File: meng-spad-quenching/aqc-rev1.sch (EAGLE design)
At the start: 135 parts, among them IC1 ADCMP582, IC2 NC7SV74K8X, IC3 LT3032-5, IC4 OPA342, IC5 OPA342, IC6 LTC1711, IC7 DS1100LU-20+, IC8 LT3032-15, IC9 NC7WZ16P6X, J1 VIN_LOGIC, M1 BSS806N, Q1 MMBTH81, Q2 MMBTH81, Q3 MMBTH81, Q4 MMBTH81, Q5 MMBTH81, Q6 MMBTH81, T1 MMBTH10, T2 MMBTH10, T3 MMBTH10, T4 MMBTH10, T5 MMBTH10, T6 MMBTH10, T7 MMBTH10, U1 SN65EPT21DGK, U2 TPS78233DDCT, U3 SN65EPT22DGK, X1 CONN_SPAD, X2 CONN_PHOTON_COUNTER, X4 CONN_VREF_ONE_SHOT_EXT, X5 CONN_VREF_DIAMOND_IBIAS_EXT, X6 CONN_VREF_CASCODE_IBIAS_EXT

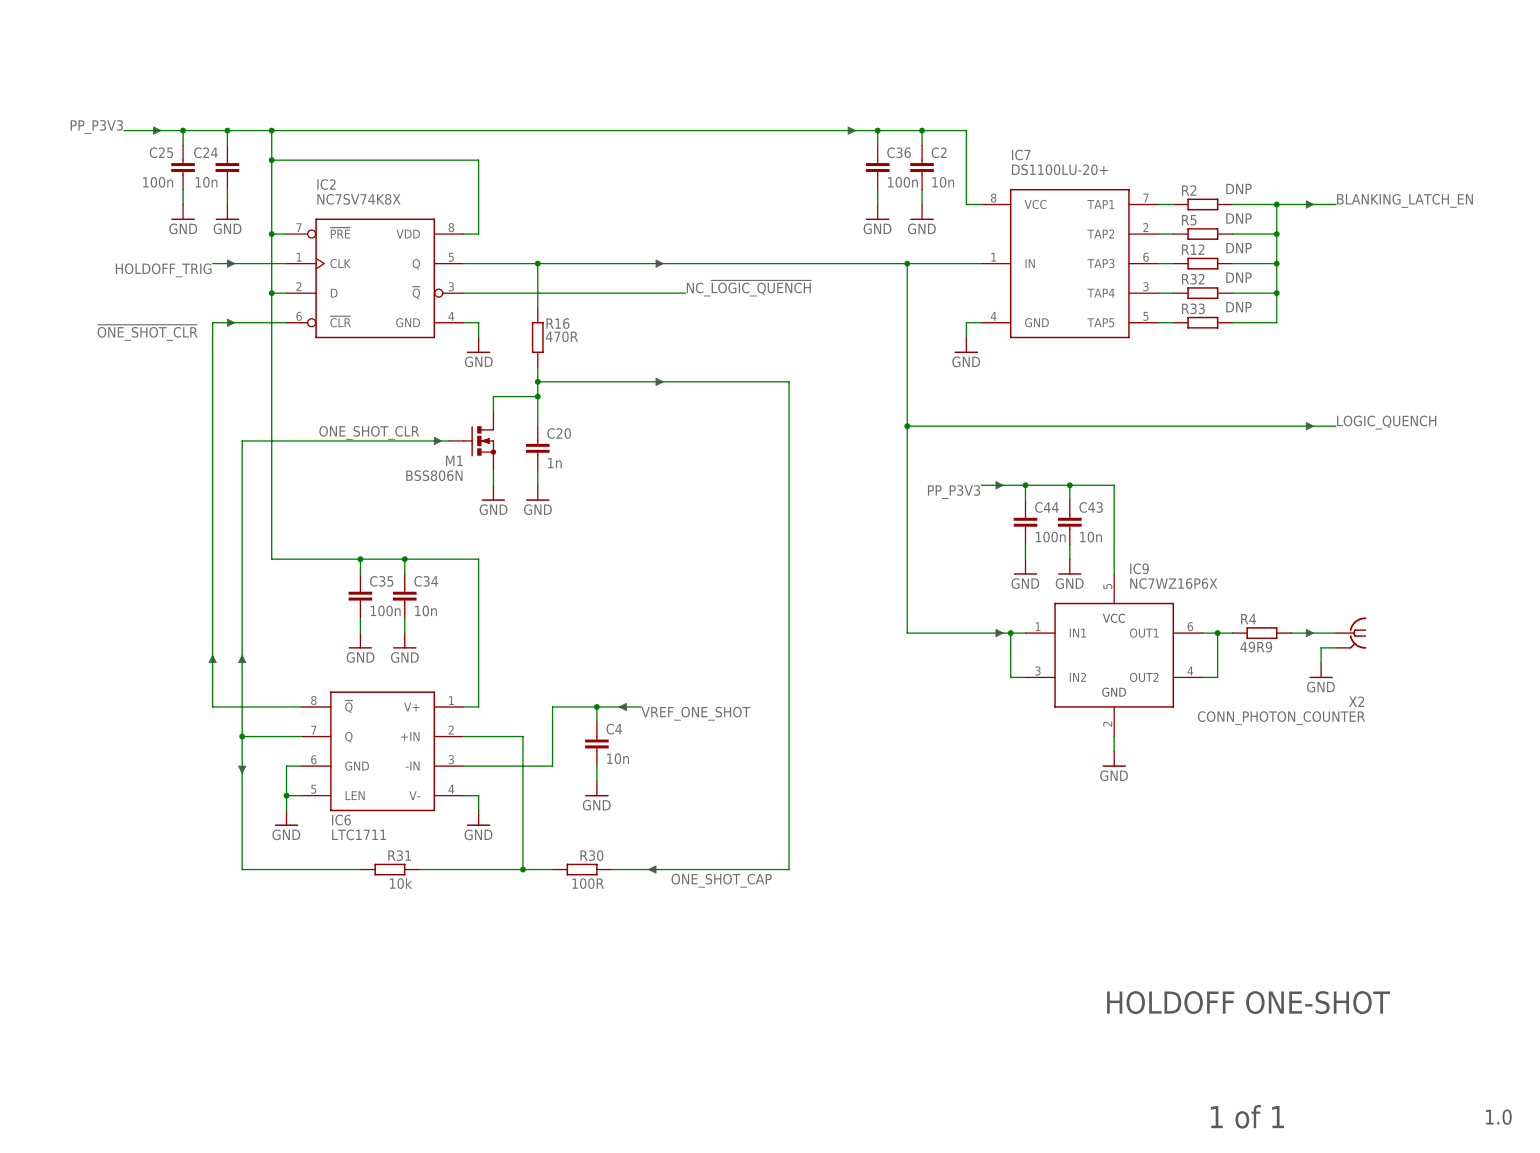
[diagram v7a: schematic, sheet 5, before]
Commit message: Added forced quenching input, finalized connector placement in layout
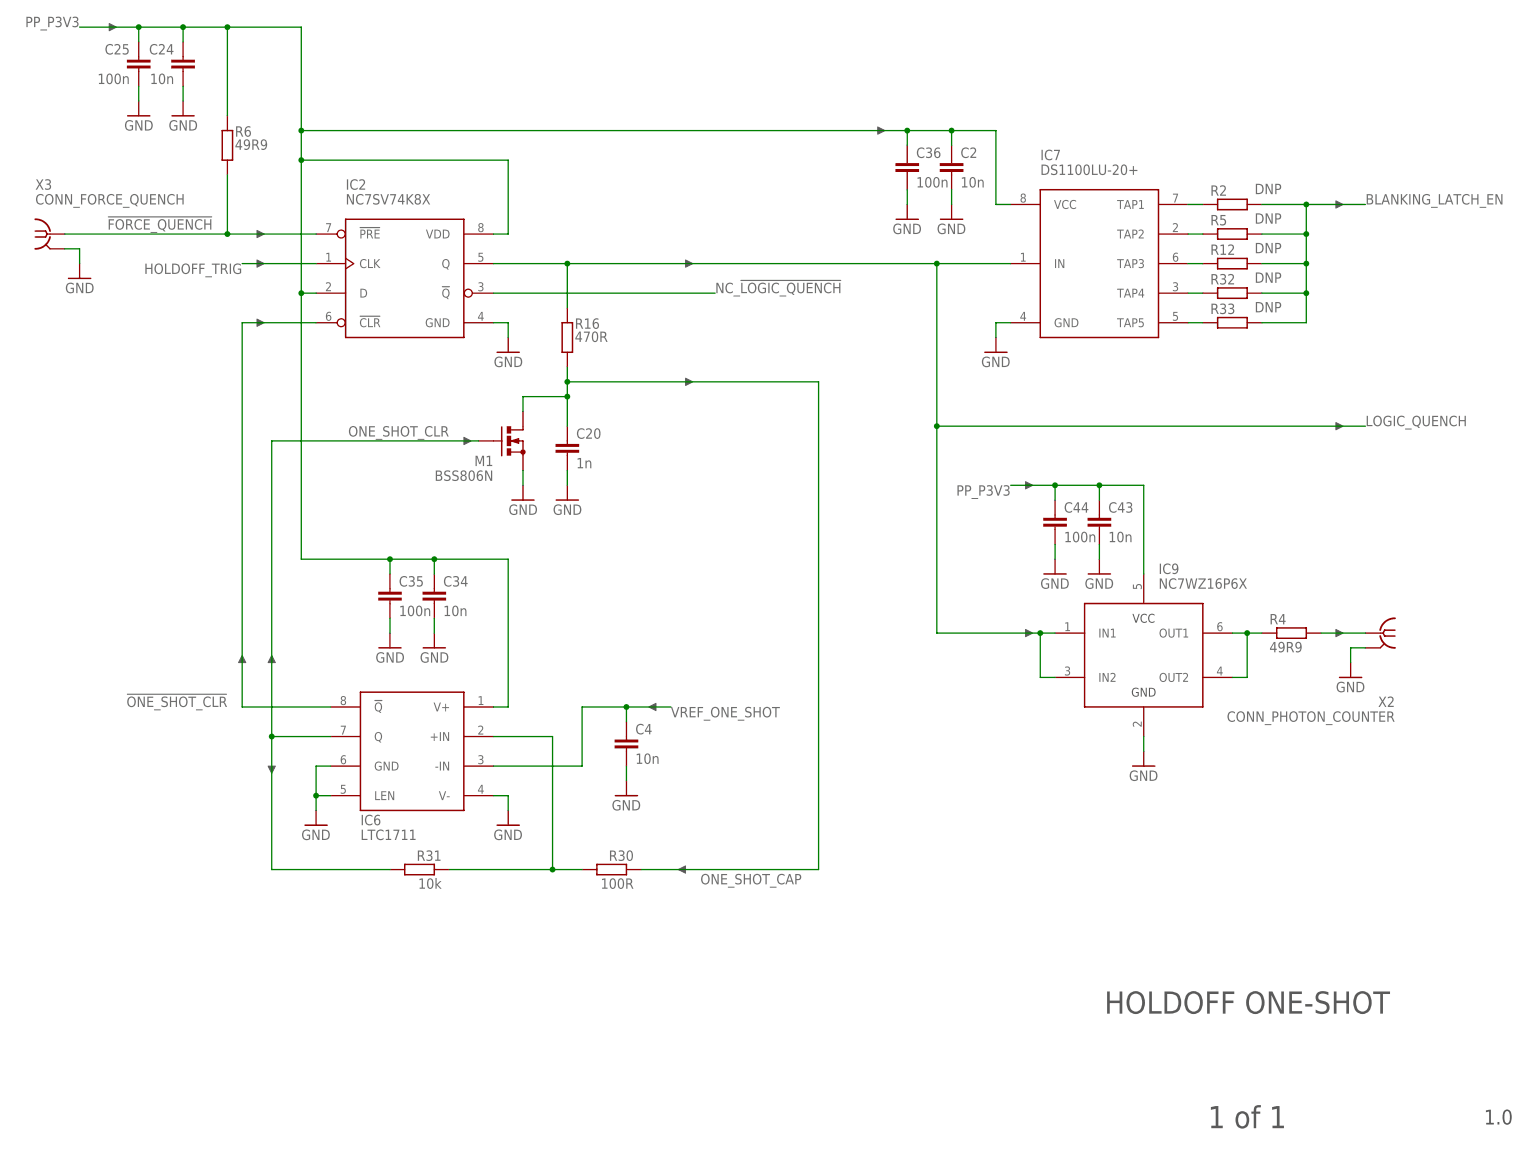
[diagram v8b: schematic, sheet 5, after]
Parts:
- added R6: 49R9, rcl:R-EU_R0603
- added X3: CONN_FORCE_QUENCH, con-coax:SMA-142-0711-871/876
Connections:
- new net !FORCE_QUENCH: IC2.!PRE, R6.1, X3G1.1
- net GND: now also X3G1.GND
- net PP_P3V3: now also R6.2; no longer IC2.!PRE
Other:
- note added: "Assert before probe has landed"
- note added: "From control logic"
- moved on the sheet: C2, C20, C24, C25, C34, C35, C36, C4, C43, C44, IC2, IC6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
